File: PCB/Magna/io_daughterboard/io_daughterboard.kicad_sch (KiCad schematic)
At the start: 13 parts, among them J101 Conn_02x10_Counter_Clockwise

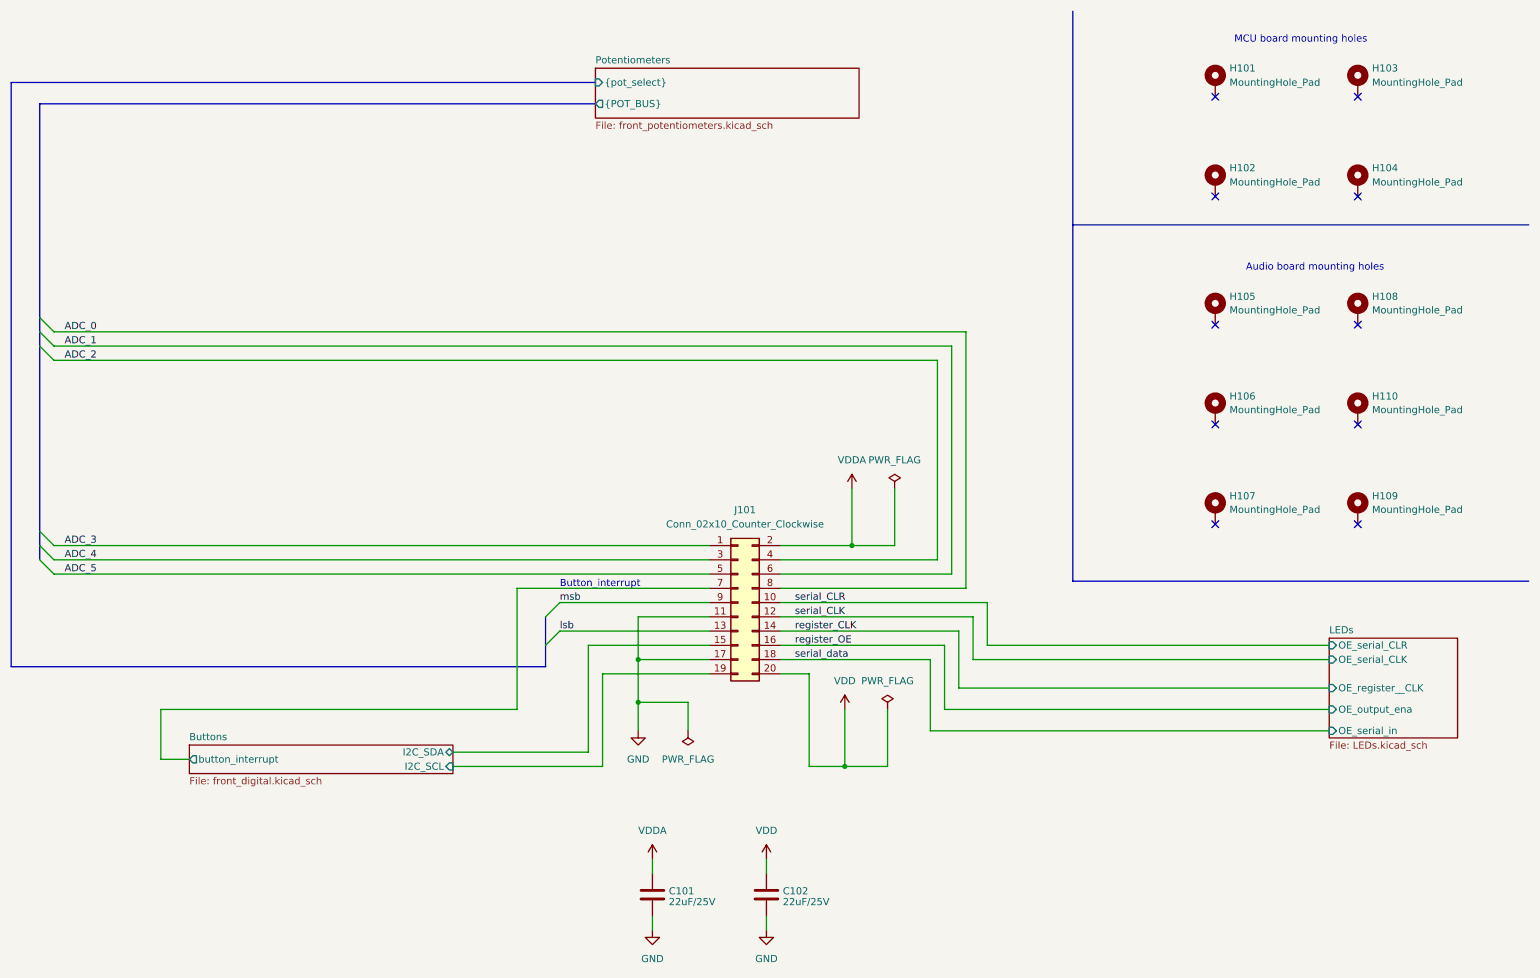
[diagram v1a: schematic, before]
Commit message: Fix board alignments and mounting holes
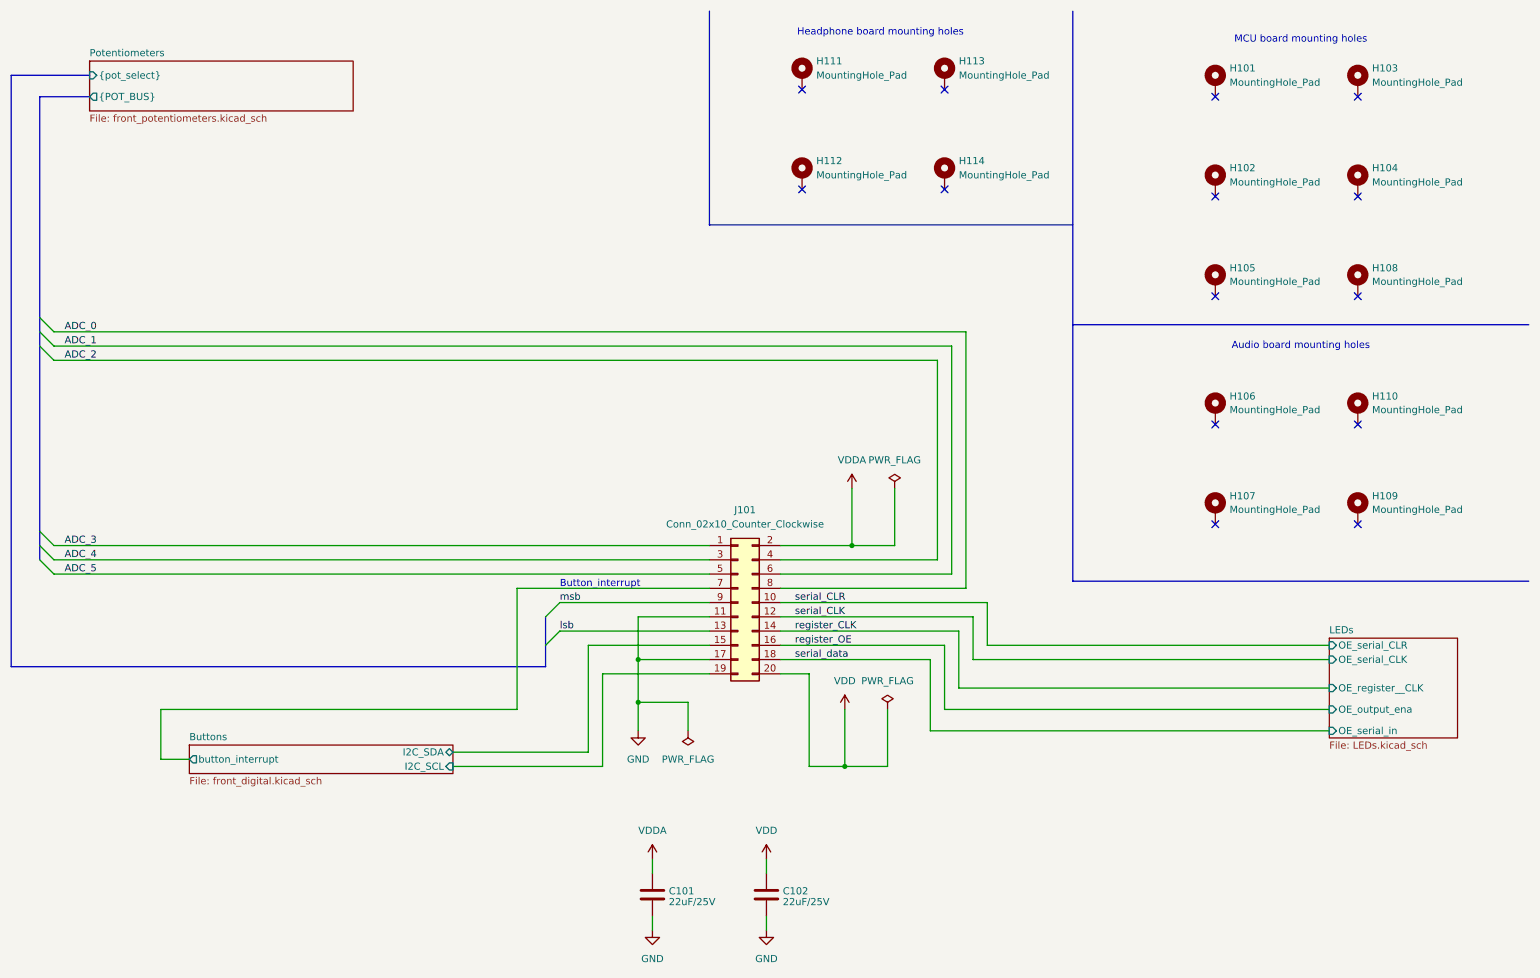
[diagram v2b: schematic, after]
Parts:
- added H111, H112, H113, H114: MountingHole_Pad, MountingHole:MountingHole_3.2mm_M3_Pad_Via, symbol Mechanical:MountingHole_Pad
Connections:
- no-connect marks 10 -> 14
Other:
- note added: "Headphone board mounting holes"
- moved on the sheet: H105, H108

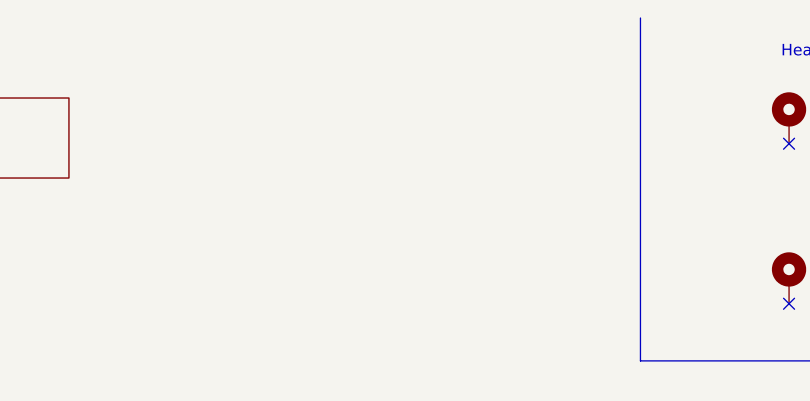
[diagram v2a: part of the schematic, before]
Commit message: Commit with small changes for production
Mainboard and IO board was manufactored with this version
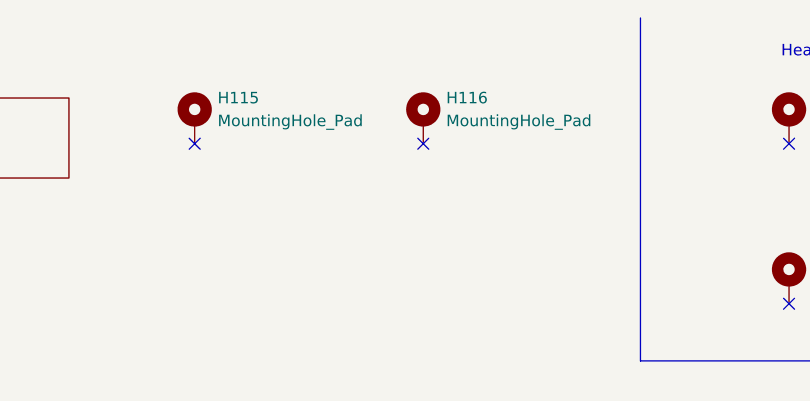
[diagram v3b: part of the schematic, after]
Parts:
- added H115, H116: MountingHole_Pad, MountingHole:MountingHole_3.2mm_M3_Pad_Via, symbol Mechanical:MountingHole_Pad
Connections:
- no-connect marks 14 -> 16
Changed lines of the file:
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@@
 	)
 	(no_connect
+		(at 88.9 26.67)
+	)
+	(no_connect
 		(at 228.6 104.14)
 	)
 	(no_connect
+		(at 114.3 26.67)
+	)
+	(no_connect
 		(at 254 45.72)
 	)
@@
 	(symbol
 		(lib_id "Mechanical:MountingHole_Pad")
+		(at 114.3 24.13 0)
+		(unit 1)
+		(exclude_from_sim no)
+		(in_bom yes)
+		(on_board yes)
+		(dnp no)
+		(fields_autoplaced yes)
+		(property "Reference" "H116"
+			(at 116.84 21.59 0)
+			(effects
+				(font
+					(size 1.27 1.27)
+				)
+				(justify left)
+			)
+		)
+		(property "Value" "MountingHole_Pad"
+			(at 116.84 24.13 0)
+			(effects
+				(font
+					(size 1.27 1.27)
+				)
+				(justify left)
+			)
+		)
+		(property "Footprint" "MountingHole:MountingHole_3.2mm_M3_Pad_Via"
+			(at 114.3 24.13 0)
+			(effects
+				(font
+					(size 1.27 1.27)
+				)
+				(hide yes)
+			)
+		)
+		(property "Datasheet" "~"
+			(at 114.3 24.13 0)
+			(effects
+				(font
+					(size 1.27 1.27)
+				)
+				(hide yes)
+			)
+		)
+		(property "Description" "Mounting Hole with connection"
+			(at 114.3 24.13 0)
+			(effects
+				(font
+					(size 1.27 1.27)
+				)
+				(hide yes)
+			)
+		)
+		(pin "1"
+		)
+		(instances
+			(project "io_daughterboard"
+				(path "/ad211228-4c3e-4f95-b724-9dfcdf1751b2"
+					(reference "H116")
+					(unit 1)
+				)
+			)
+		)
+	)
+	(symbol
+		(lib_id "Mechanical:MountingHole_Pad")
 		(at 228.6 60.96 0)
 		(unit 1)
@@
 		)
 	)
+	(symbol
+		(lib_id "Mechanical:MountingHole_Pad")
+		(at 88.9 24.13 0)
+		(unit 1)
+		(exclude_from_sim no)
+		(in_bom yes)
+		(on_board yes)
+		(dnp no)
+		(fields_autoplaced yes)
+		(property "Reference" "H115"
+			(at 91.44 21.59 0)
+			(effects
+				(font
+					(size 1.27 1.27)
+				)
+				(justify left)
+			)
+		)
+		(property "Value" "MountingHole_Pad"
+			(at 91.44 24.13 0)
+			(effects
+				(font
+					(size 1.27 1.27)
+				)
+				(justify left)
+			)
+		)
+		(property "Footprint" "MountingHole:MountingHole_3.2mm_M3_Pad_Via"
+			(at 88.9 24.13 0)
+			(effects
+				(font
+					(size 1.27 1.27)
+				)
+				(hide yes)
+			)
+		)
+		(property "Datasheet" "~"
+			(at 88.9 24.13 0)
+			(effects
+				(font
+					(size 1.27 1.27)
+				)
+				(hide yes)
+			)
+		)
+		(property "Description" "Mounting Hole with connection"
+			(at 88.9 24.13 0)
+			(effects
+				(font
+					(size 1.27 1.27)
+				)
+				(hide yes)
+			)
+		)
+		(pin "1"
+		)
+		(instances
+			(project "io_daughterboard"
+				(path "/ad211228-4c3e-4f95-b724-9dfcdf1751b2"
+					(reference "H115")
+					(unit 1)
+				)
+			)
+		)
+	)
 	(sheet
 		(at 248.92 124.46)
@@
 				)
 			)
-			(project "io_daughterboard-rounded"
+			(project "io_daughterboard"
 				(path "/ad211228-4c3e-4f95-b724-9dfcdf1751b2"
 					(page "2")
@@
 				)
 			)
-			(project "io_daughterboard-rounded"
+			(project "io_daughterboard"
 				(path "/ad211228-4c3e-4f95-b724-9dfcdf1751b2"
 					(page "3")
@@
 				)
 			)
-			(project "io_daughterboard-rounded"
+			(project "io_daughterboard"
 				(path "/ad211228-4c3e-4f95-b724-9dfcdf1751b2"
 					(page "4")
